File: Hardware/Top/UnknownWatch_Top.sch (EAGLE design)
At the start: 55 parts, among them SW1 SWITCH.MOM, SW2 SWITCH.MOM, SW6 SWITCH.MOM, U2 NRF52832_MODULE_MDBT42, U4 PCF8523, U5 PHOTOTRANSISTOR

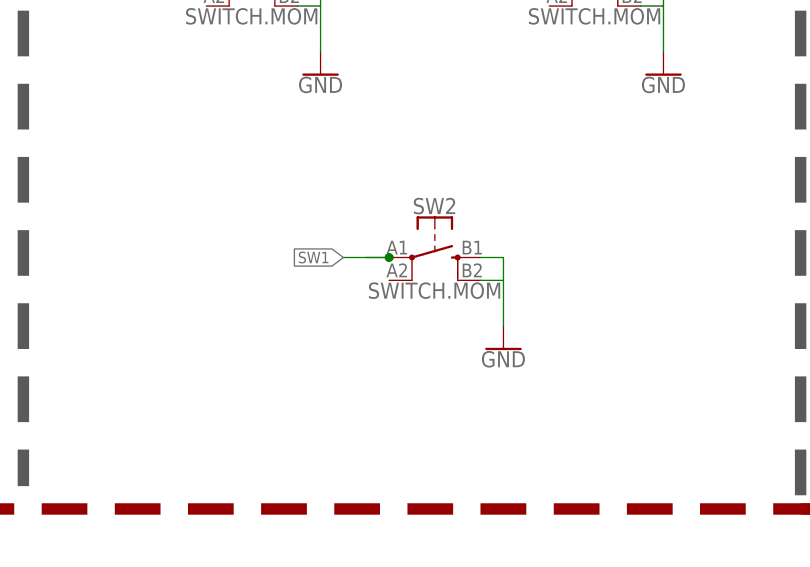
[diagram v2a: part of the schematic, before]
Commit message: Deleted a button
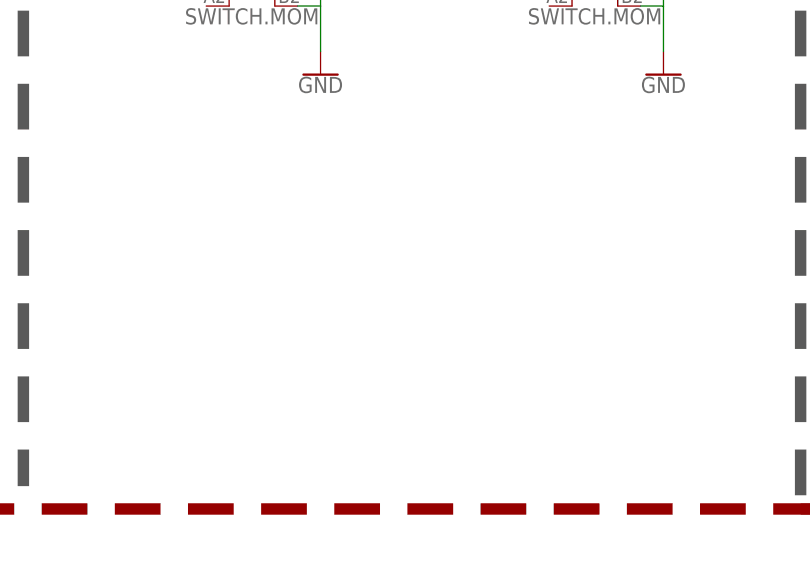
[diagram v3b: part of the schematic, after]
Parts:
- removed SW2: SWITCH.MOM, LinnesLab-Switches:SWITCH.MOM
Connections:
- net GND: no longer SW2.3, SW2.4
- net SW1: no longer SW2.1
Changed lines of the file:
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@@
 <part name="SW1" library="LinnesLab-Switches" deviceset="SWITCH.MOM" device=""/>
 <part name="GND6" library="LinnesLab-Symbols" deviceset="GND" device=""/>
-<part name="SW2" library="LinnesLab-Switches" deviceset="SWITCH.MOM" device=""/>
-<part name="GND13" library="LinnesLab-Symbols" deviceset="GND" device=""/>
 </parts>
 <sheets>
@@
 <attribute name="VALUE" x="411.48" y="-51.054" size="1.778" layer="96" align="top-center"/>
 </instance>
-<instance part="SW2" gate="G$1" x="386.08" y="-71.12" smashed="yes">
-<attribute name="NAME" x="386.08" y="-66.294" size="1.778" layer="95" font="vector" align="bottom-center"/>
-<attribute name="VALUE" x="386.08" y="-73.914" size="1.778" layer="96" font="vector" align="top-center"/>
-</instance>
-<instance part="GND13" gate="G$1" x="393.7" y="-81.28" smashed="yes">
-<attribute name="VALUE" x="393.7" y="-81.534" size="1.778" layer="96" align="top-center"/>
-</instance>
 </instances>
 <busses>
@@
 <wire x1="411.48" y1="-43.18" x2="408.94" y2="-43.18" width="0.1524" layer="91"/>
 <pinref part="GND6" gate="G$1" pin="GND"/>
-</segment>
-<segment>
-<pinref part="SW2" gate="G$1" pin="3"/>
-<wire x1="391.16" y1="-71.12" x2="393.7" y2="-71.12" width="0.1524" layer="91"/>
-<wire x1="393.7" y1="-71.12" x2="393.7" y2="-73.66" width="0.1524" layer="91"/>
-<pinref part="SW2" gate="G$1" pin="4"/>
-<wire x1="393.7" y1="-78.74" x2="393.7" y2="-73.66" width="0.1524" layer="91"/>
-<wire x1="393.7" y1="-73.66" x2="391.16" y2="-73.66" width="0.1524" layer="91"/>
-<pinref part="GND13" gate="G$1" pin="GND"/>
 </segment>
 </net>
@@
 <junction x="398.78" y="-40.64"/>
 </segment>
-<segment>
-<pinref part="SW2" gate="G$1" pin="1"/>
-<wire x1="381" y1="-71.12" x2="378.46" y2="-71.12" width="0.1524" layer="91"/>
-<label x="375.92" y="-71.12" size="1.27" layer="95" rot="R180" xref="yes"/>
-<wire x1="375.92" y1="-71.12" x2="381" y2="-71.12" width="0.1524" layer="91"/>
-<junction x="381" y="-71.12"/>
-</segment>
-</net>
+</net>

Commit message: Added connections from bottom to top board and other various changes.
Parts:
- removed C11: 300p, LinnesLab-Passives:CAPACITOR0603
- removed C12: 10u, LinnesLab-Passives:CAPACITOR0805
- removed C14: 100n, LinnesLab-Passives:CAPACITOR0603
- removed C7: 1u, LinnesLab-Passives:CAPACITOR0603
- removed CORTEX1: CORTEX_DEBUG_PTH, LinnesLab-Connectors:CORTEX_DEBUG_PTH
- removed D1: (no value), LinnesLab-DiscreteSemi:SCHOTTKY-USC
- removed L2: 10u, LinnesLab-Passives:INDUCTOR0603
- removed R8, R9: 10k, LinnesLab-Passives:RESISTOR0603
- removed SW3, SW4: (no value), LinnesLab-Switches:SPST-PTS830GG140-COPY.1-3
- removed XTAL3: 32.7680kHz, LinnesLab-Clocks:CRYSTALECS-.327-12.5-12-C-TR
- added C27: 1u, LinnesLab-Passives:CAPACITOR0603
- added C28, C29: (no value), LinnesLab-Passives:CAPACITOR0603
- added C30, C31: 300p, LinnesLab-Passives:CAPACITOR0603
- added C32: 10u, LinnesLab-Passives:CAPACITOR0805
- added C33: 100n, LinnesLab-Passives:CAPACITOR0603
- added CORTEX3: CORTEX_DEBUG_PTH, LinnesLab-Connectors:CORTEX_DEBUG_PTH
- added D3: (no value), LinnesLab-DiscreteSemi:SCHOTTKY-USC
- added J1: (no value), LinnesLab-Connectors:CONN_07
- added JP2: (no value), LinnesLab-Switches:JUMPER-SMT_2_NO_SILK
- added L3: 10u, LinnesLab-Passives:INDUCTOR0603
- added LED5: RED, LinnesLab-LED:LED0603
- added LED6: BLUE, LinnesLab-LED:LED0603
- added R1: 0, LinnesLab-Passives:RESISTOR0603
- added R10, R16: 27, LinnesLab-Passives:RESISTOR0603
- added R17, R18, R20, R21: 1k, LinnesLab-Passives:RESISTOR0603
- added R19: 10k, LinnesLab-Passives:RESISTOR0603
- added SW7, SW8: (no value), LinnesLab-Switches:SPST-PTS830GG140-COPY.1-3
- added U6: NRF52832_MODULE_MDBT42, LinnesLab-Microcontrollers:NRF52832_MODULE_MDBT42
- added XTAL4: 32.768kHz, LinnesLab-Clocks:CRYSTALECS-.327-12.5-12-C-TR
- C10: value 300p -> 47p
- C8: value (none) -> 100n
- C9: value (none) -> 47p
- LED4: value BLUE -> YELLOW
- R3: value 1k -> 0
- R4: value 1k -> 10K
- R5: value 10k -> 10K
- U2: value NRF52832_MODULE_MDBT42 -> FT231XS; device LinnesLab-Microcontrollers:NRF52832_MODULE_MDBT42 -> LinnesLab-DigitalIC:FT231XS
- XTAL2: value 32.768kHz -> 32.7680kHz; FREQ (none) -> 32.7680KHZ
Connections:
- removed net N$10: LED4.A, R4.1
- removed net N$19: U4.OSCO, XTAL3.1
- removed net N$20: U4.OSCI, XTAL3.2
- removed net N$4: C8.2, U2.P0.00/XL1, XTAL2.1
- removed net RXD: U2.P0.08
- removed net TXD: U2.P0.06
- new net !CTS: JP2.2, U2.!CTS
- new net FT3V3: U2.3V3OUT
- new net N$16: LED4.C, R21.2
- new net N$26: C28.2, U6.P0.00/XL1, XTAL4.1
- new net N$27: C29.1, U6.P0.01/XL2, XTAL4.2
- new net N$28: LED5.A, R17.1
- new net N$29: LED6.A, R18.1
- new net N$30: L3.1, U6.DCC
- new net N$31: C27.1, L3.2, U6.DEC4
- new net N$32: CORTEX3.NC/TDI
- new net RXD.FT: R3.1, U2.RXD
- new net RXD.NRF: R1.2, U6.P0.08
- new net RXLED: R20.1, U2.CBUS1
- new net TXD.FT: R1.1, U2.TXD
- new net TXD.NRF: R3.2, U6.P0.06
- new net TXLED: R21.1, U2.CBUS2
- net 3.3V: now also C32.2, C8.2, CORTEX3.VCC, D3.C, LED3.A, LED4.A, R19.2, R4.2, U2.!RESET, U2.VCCIO, U6.VDD; no longer C12.2, CORTEX1.VCC, D1.C, R8.2, R9.2, U2.VDD
- net DFU: now also SW7.B, U6.P0.20; no longer SW3.B, U2.P0.20
- net DTR: now also C33.1, U2.!DTR; no longer C14.1
- net FRST: now also U6.P0.22; no longer U2.P0.22
- net GND: now also C10.1, C27.2, C28.1, C29.2, C30.2, C31.2, C32.1, CORTEX3.GND@3, CORTEX3.GND@5, CORTEX3.GNDDTCT, CORTEX3.KEY, JP2.1, LED5.C, LED6.C, SW7.A, SW8.B, U2.GND@16, U2.GND@6, U6.GND@1, U6.GND@2, U6.GND@3, U6.GND@4; no longer C10.2, C11.2, C12.1, C7.2, CORTEX1.GND@3, CORTEX1.GND@5, CORTEX1.GNDDTCT, CORTEX1.KEY, LED3.C, LED4.C, SW3.A, SW4.B, U2.GND@1, U2.GND@2, U2.GND@3, U2.GND@4
- net LED1: now also R17.2, U6.P0.17; no longer R3.2, U2.P0.17
- net LED2: now also R18.2, U6.P0.19; no longer R4.2, U2.P0.19
- net MISO: now also U6.P0.14; no longer U2.P0.14
- net MOSI: now also U6.P0.13; no longer U2.P0.13
- net N$11: now also R10.2, U2.USBDM; no longer L2.1, U2.DCC
- net N$12: now also R16.2, U2.USBDP; no longer C7.1, L2.2, U2.DEC4
- net N$14: now also LED3.C, R20.2; no longer CORTEX1.NC/TDI
- net N$6: now also U4.OSCO, XTAL2.1; no longer C9.1, U2.P0.01/XL2, XTAL2.2
- net N$9: now also U4.OSCI, XTAL2.2; no longer LED3.A, R3.1
- net P0.09/NFC1: now also C31.1, U6.P0.09; no longer C11.1, U2.P0.09
- net P0.10/NFC2: now also C30.1, U6.P0.10; no longer C10.1, U2.P0.10
- net RESET: now also C33.2, CORTEX3.!RESET, D3.A, R19.1, SW8.A, U6.P0.21/RESET; no longer C14.2, CORTEX1.!RESET, D1.A, R5.1, SW4.A, U2.P0.21/RESET
- net SCK: now also U6.P0.12; no longer U2.P0.12
- net SCL: now also R5.1, U6.P0.26; no longer R8.1, U2.P0.26
- net SDA: now also R4.1, U6.P0.25; no longer R9.1, U2.P0.25
- net SWCLK: now also CORTEX3.SWDCLK/TCK, U6.SWDCLK; no longer CORTEX1.SWDCLK/TCK, U2.SWDCLK
- net SWDIO: now also CORTEX3.SWDIO/TMS, U6.SWDIO; no longer CORTEX1.SWDIO/TMS, U2.SWDIO
- net SWO: now also CORTEX3.SWO/TDO, U6.P0.18/SWO; no longer CORTEX1.SWO/TDO, U2.P0.18/SWO
- net USB+: now also C9.1, R16.1
- net USB-: now also C10.2, R10.1
- net V_USB: now also U2.VCC
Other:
- note added: "FTDI Serial-to-USB Converter"
- note added: "I don't remember if CTS needs to be grounded or left floating so here's a jumper to ground so it can be configued either way dynamically."
- note added: "TXD goes to RX on the other device RXD goes to TX on the other device"
- note removed: "RTC"
- moved on the sheet: C10, C2, C8, C9, LED3, LED4, R3, R4, R5, U4, XTAL2

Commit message: Made all changes associated wih take 002
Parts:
- renumbered SW1 to SW2
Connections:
- removed net BATT: R13.1, R14.2
- removed net CD1: SD2.CARD_DETECT
- removed net CHRG.STAT: CHRG2.STAT, R12.1
- removed net CS.OLED: U3./CS
- removed net DC.OLED: U3.DC/I2C_SA0
- removed net RESET.OLED: U3./RES
- removed net SD.CS: SD2.CS
- removed net SW1: SW2.1, SW6.1
- new net A4/BATT: R13.1, R14.2, U6.P0.28/AIN4
- new net A6/TIA: U6.P0.30/AIN6
- new net A7/PPG: U6.P0.31/AIN7
- new net D11/SW1: SW6.1, U6.P0.11
- new net D15/SW2: SW2.1, U6.P0.15
- new net D16/CS.OLED: U3./CS, U6.P0.16
- new net D27/CHRG.STATUS: CHRG2.STAT, R12.1, U6.P0.27
- new net D29/LED.CTRL: U6.P0.29/AIN5
- new net D3/RESET.OLED: U3./RES, U6.P0.03/AIN1
- new net D4/DC.OLED: U3.DC/I2C_SA0, U6.P0.04/AIN2
- new net D5/CD1: SD2.CARD_DETECT, U6.P0.05/AIN3
- new net D7/SD.CS: SD2.CS, U6.P0.07

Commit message: Began routing top board.
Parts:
- removed C3: 2.2u, LinnesLab-Passives:CAPACITOR0603
- removed J1: (no value), LinnesLab-Connectors:CONN_07
- removed R2: 10k, LinnesLab-Passives:RESISTOR0603
- removed U5: PHOTOTRANSISTOR, LinnesLab-Sensors:PHOTOTRANSISTOR
- added J3: (no value), LinnesLab-Connectors:CONN_07-1.27MM
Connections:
- removed net OUTPUT: C3.1, R2.2, U5.E
- net 3.3V: now also J3.4; no longer U5.C
- net A6/TIA: now also J3.6
- net A7/PPG: now also J3.7
- net D29/LED.CTRL: now also J3.5
- net GND: now also J3.3; no longer C3.2, R2.1
- net SCL: now also J3.2
- net SDA: now also J3.1
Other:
- note added: "Connection to bottom board"
- note removed: "Ambient Light Sensor"
- note removed: "Outputs a voltage relative to incident light. Will need to calibrate RL to based on the desired dynamic range."

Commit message: Complted all routing of top board associated with take 4.
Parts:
- removed C30, C31: 300p, LinnesLab-Passives:CAPACITOR0603
- removed R15: 100k, LinnesLab-Passives:RESISTOR0603
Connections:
- net 3.3V: no longer R15.2
- net GND: no longer C30.2, C31.2, R15.1, SW2.4, SW6.4
- net P0.09/NFC1: no longer C31.1
- net P0.10/NFC2: no longer C30.1
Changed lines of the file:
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@@
 <part name="SUPPLY16" library="LinnesLab-Symbols" deviceset="VLIPO" device=""/>
 <part name="GND43" library="LinnesLab-Symbols" deviceset="GND" device=""/>
-<part name="R15" library="LinnesLab-Passives" deviceset="RESISTOR" device="0603" package3d_urn="urn:adsk.eagle:package:15661944/2" value="100k"/>
-<part name="GND44" library="LinnesLab-Symbols" deviceset="GND" device=""/>
 <part name="SUPPLY17" library="LinnesLab-Symbols" deviceset="VIN" device=""/>
 <part name="SW6" library="LinnesLab-Switches" deviceset="SWITCH.MOM" device=""/>
@@
 <part name="GND55" library="LinnesLab-Symbols" deviceset="GND" device=""/>
 <part name="GND56" library="LinnesLab-Symbols" deviceset="GND" device=""/>
-<part name="GND57" library="LinnesLab-Symbols" deviceset="GND" device=""/>
-<part name="GND58" library="LinnesLab-Symbols" deviceset="GND" device=""/>
 <part name="GND59" library="LinnesLab-Symbols" deviceset="GND" device=""/>
 <part name="GND60" library="LinnesLab-Symbols" deviceset="GND" device=""/>
@@
 <part name="C28" library="LinnesLab-Passives" deviceset="CAPACITOR" device="0603" package3d_urn="urn:adsk.eagle:package:15661989/2"/>
 <part name="C29" library="LinnesLab-Passives" deviceset="CAPACITOR" device="0603" package3d_urn="urn:adsk.eagle:package:15661989/2"/>
-<part name="C30" library="LinnesLab-Passives" deviceset="CAPACITOR" device="0603" package3d_urn="urn:adsk.eagle:package:15661989/2" value="300p"/>
-<part name="C31" library="LinnesLab-Passives" deviceset="CAPACITOR" device="0603" package3d_urn="urn:adsk.eagle:package:15661989/2" value="300p"/>
 <part name="C32" library="LinnesLab-Passives" deviceset="CAPACITOR" device="0805" package3d_urn="urn:adsk.eagle:package:15662010/2" value="10u"/>
 <part name="L3" library="LinnesLab-Passives" deviceset="INDUCTOR" device="0603" override_package3d_urn="urn:adsk.eagle:package:18592195/2" override_package_urn="urn:adsk.eagle:footprint:18592196/1" value="10u"/>
@@
 <attribute name="VALUE" x="76.2" y="-71.374" size="1.778" layer="96" align="top-center"/>
 </instance>
-<instance part="R15" gate="G$1" x="88.9" y="-35.56" smashed="yes" rot="R90">
-<attribute name="NAME" x="87.4014" y="-39.37" size="1.778" layer="95" rot="R90"/>
-<attribute name="VALUE" x="92.202" y="-39.37" size="1.778" layer="96" rot="R90"/>
-</instance>
-<instance part="GND44" gate="G$1" x="88.9" y="-45.72" smashed="yes">
-<attribute name="VALUE" x="88.9" y="-45.974" size="1.778" layer="96" align="top-center"/>
-</instance>
 <instance part="SUPPLY17" gate="G$1" x="30.48" y="-25.4" smashed="yes">
 <attribute name="VALUE" x="30.48" y="-22.606" size="1.778" layer="96" align="bottom-center"/>
@@
 <attribute name="VALUE" x="101.6" y="81.026" size="1.778" layer="96" align="top-center"/>
 </instance>
-<instance part="GND57" gate="G$1" x="104.14" y="50.8" smashed="yes">
-<attribute name="VALUE" x="104.14" y="50.546" size="1.778" layer="96" align="top-center"/>
-</instance>
-<instance part="GND58" gate="G$1" x="91.44" y="50.8" smashed="yes">
-<attribute name="VALUE" x="91.44" y="50.546" size="1.778" layer="96" align="top-center"/>
-</instance>
 <instance part="GND59" gate="G$1" x="81.28" y="50.8" smashed="yes">
 <attribute name="VALUE" x="81.28" y="50.546" size="1.778" layer="96" align="top-center"/>
@@
 <attribute name="NAME" x="82.804" y="61.341" size="1.778" layer="95"/>
 <attribute name="VALUE" x="82.804" y="56.261" size="1.778" layer="96"/>
-</instance>
-<instance part="C30" gate="G$1" x="104.14" y="58.42" smashed="yes">
-<attribute name="NAME" x="105.664" y="61.341" size="1.778" layer="95"/>
-<attribute name="VALUE" x="105.664" y="56.261" size="1.778" layer="96"/>
-</instance>
-<instance part="C31" gate="G$1" x="91.44" y="58.42" smashed="yes">
-<attribute name="NAME" x="92.964" y="61.341" size="1.778" layer="95"/>
-<attribute name="VALUE" x="92.964" y="56.261" size="1.778" layer="96"/>
 </instance>
 <instance part="C32" gate="G$1" x="60.96" y="93.98" smashed="yes" rot="R180">
@@
 </segment>
 <segment>
-<pinref part="R15" gate="G$1" pin="1"/>
-<pinref part="GND44" gate="G$1" pin="GND"/>
-<wire x1="88.9" y1="-43.18" x2="88.9" y2="-40.64" width="0.1524" layer="91"/>
-</segment>
-<segment>
 <pinref part="SW6" gate="G$1" pin="3"/>
 <wire x1="370.84" y1="-40.64" x2="373.38" y2="-40.64" width="0.1524" layer="91"/>
-<wire x1="373.38" y1="-40.64" x2="373.38" y2="-43.18" width="0.1524" layer="91"/>
-<pinref part="SW6" gate="G$1" pin="4"/>
-<wire x1="373.38" y1="-48.26" x2="373.38" y2="-43.18" width="0.1524" layer="91"/>
-<wire x1="373.38" y1="-43.18" x2="370.84" y2="-43.18" width="0.1524" layer="91"/>
+<wire x1="373.38" y1="-48.26" x2="373.38" y2="-40.64" width="0.1524" layer="91"/>
 <pinref part="GND1" gate="G$1" pin="GND"/>
 </segment>
@@
 <pinref part="SW2" gate="G$1" pin="3"/>
 <wire x1="408.94" y1="-40.64" x2="411.48" y2="-40.64" width="0.1524" layer="91"/>
-<wire x1="411.48" y1="-40.64" x2="411.48" y2="-43.18" width="0.1524" layer="91"/>
-<pinref part="SW2" gate="G$1" pin="4"/>
-<wire x1="411.48" y1="-48.26" x2="411.48" y2="-43.18" width="0.1524" layer="91"/>
-<wire x1="411.48" y1="-43.18" x2="408.94" y2="-43.18" width="0.1524" layer="91"/>
+<wire x1="411.48" y1="-48.26" x2="411.48" y2="-40.64" width="0.1524" layer="91"/>
 <pinref part="GND6" gate="G$1" pin="GND"/>
 </segment>
@@
 <pinref part="GND60" gate="G$1" pin="GND"/>
 <pinref part="C28" gate="G$1" pin="1"/>
-</segment>
-<segment>
-<pinref part="C31" gate="G$1" pin="2"/>
-<pinref part="GND58" gate="G$1" pin="GND"/>
-<wire x1="91.44" y1="53.34" x2="91.44" y2="55.88" width="0.1524" layer="91"/>
-</segment>
-<segment>
-<pinref part="C30" gate="G$1" pin="2"/>
-<pinref part="GND57" gate="G$1" pin="GND"/>
-<wire x1="104.14" y1="53.34" x2="104.14" y2="55.88" width="0.1524" layer="91"/>
 </segment>
 <segment>
@@
 <wire x1="78.74" y1="-25.4" x2="78.74" y2="-27.94" width="0.1524" layer="91"/>
 <junction x="78.74" y="-27.94"/>
-<wire x1="78.74" y1="-27.94" x2="88.9" y2="-27.94" width="0.1524" layer="91"/>
-<pinref part="R15" gate="G$1" pin="2"/>
-<wire x1="88.9" y1="-27.94" x2="88.9" y2="-30.48" width="0.1524" layer="91"/>
 </segment>
 <segment>
@@
 <segment>
 <wire x1="96.52" y1="86.36" x2="96.52" y2="66.04" width="0.1524" layer="91"/>
-<wire x1="91.44" y1="66.04" x2="96.52" y2="66.04" width="0.1524" layer="91"/>
-<wire x1="91.44" y1="66.04" x2="91.44" y2="63.5" width="0.1524" layer="91"/>
-<pinref part="C31" gate="G$1" pin="1"/>
 <pinref part="U6" gate="G$1" pin="P0.09"/>
 <label x="96.52" y="68.58" size="1.27" layer="95" rot="R180" xref="yes"/>
@@
 <segment>
 <wire x1="99.06" y1="86.36" x2="99.06" y2="66.04" width="0.1524" layer="91"/>
-<wire x1="99.06" y1="66.04" x2="104.14" y2="66.04" width="0.1524" layer="91"/>
-<wire x1="104.14" y1="66.04" x2="104.14" y2="63.5" width="0.1524" layer="91"/>
-<pinref part="C30" gate="G$1" pin="1"/>
 <pinref part="U6" gate="G$1" pin="P0.10"/>
 <label x="99.06" y="68.58" size="1.27" layer="95" xref="yes"/>

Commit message: Completed take 5 and did part of take 6.
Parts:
- removed C2, C5, C6: 1u, LinnesLab-Passives:CAPACITOR0603
- removed C20, C21: 4.7u, LinnesLab-Passives:CAPACITOR0603
- removed CHRG2: MCP73831, LinnesLab-Power:MCP73831
- removed LDO2: MIC5504, LinnesLab-Power:MIC5504
- removed R11: (no value), LinnesLab-Passives:RESISTOR0603
- removed R12: 100k, LinnesLab-Passives:RESISTOR0603
- removed SD2: (no value), LinnesLab-Connectors:MICROSD
- removed U4: PCF8523, LinnesLab-Clocks:PCF8523
- removed XTAL2: 32.7680kHz, LinnesLab-Clocks:CRYSTALECS-.327-12.5-12-C-TR
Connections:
- removed net CD2: SD2.CARD_DETECT1
- removed net N$17: CHRG2.PROG, R11.2
- removed net N$6: U4.OSCO, XTAL2.1
- removed net N$9: U4.OSCI, XTAL2.2
- net 3.3V: no longer C2.1, C6.1, LDO2.OUT, SD2.VDD, U4.VDD
- net D27/CHRG.STATUS: no longer CHRG2.STAT, R12.1
- net D5/CD1: no longer SD2.CARD_DETECT
- net D7/SD.CS: no longer SD2.CS
- net GND: no longer C2.2, C20.2, C21.1, C5.1, C6.2, CHRG2.VSS, LDO2.GND, R11.1, SD2.GND, SD2.GND1, SD2.VSS, U4.VSS
- net MISO: no longer SD2.DATA_OUT
- net MOSI: no longer SD2.DATA_IN
- net SCK: no longer SD2.SCLK
- net SCL: no longer U4.SCL
- net SDA: no longer U4.SDA
- net VIN: no longer C21.2, C5.2, CHRG2.VIN, LDO2.EN, LDO2.IN, R12.2
- net VLIPO: no longer C20.1, CHRG2.VBAT
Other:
- note removed: "Back-up battery if desired"
- note removed: "I2C Address = 0x68h"
- note removed: "Real-Time Clock"
- note removed: "SD Card"
